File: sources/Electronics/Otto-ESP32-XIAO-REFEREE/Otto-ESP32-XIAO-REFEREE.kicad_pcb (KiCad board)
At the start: 2 copper layers, 60 x 52 mm, 48 parts, among them J1 Industrial Sensor, J12 OLED 0,91" - I2C (SKU21796), J2 Industrial Sensor, J7 Ultrasonic sensor, J8 Barrel_Jack_Switch, SW1 SW_SPDT, SW4 CherryMX, SW5 CherryMX, SW6 CherryMX, U1 MOUDLE-SEEEDUINO-XIAO-ESP32C3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

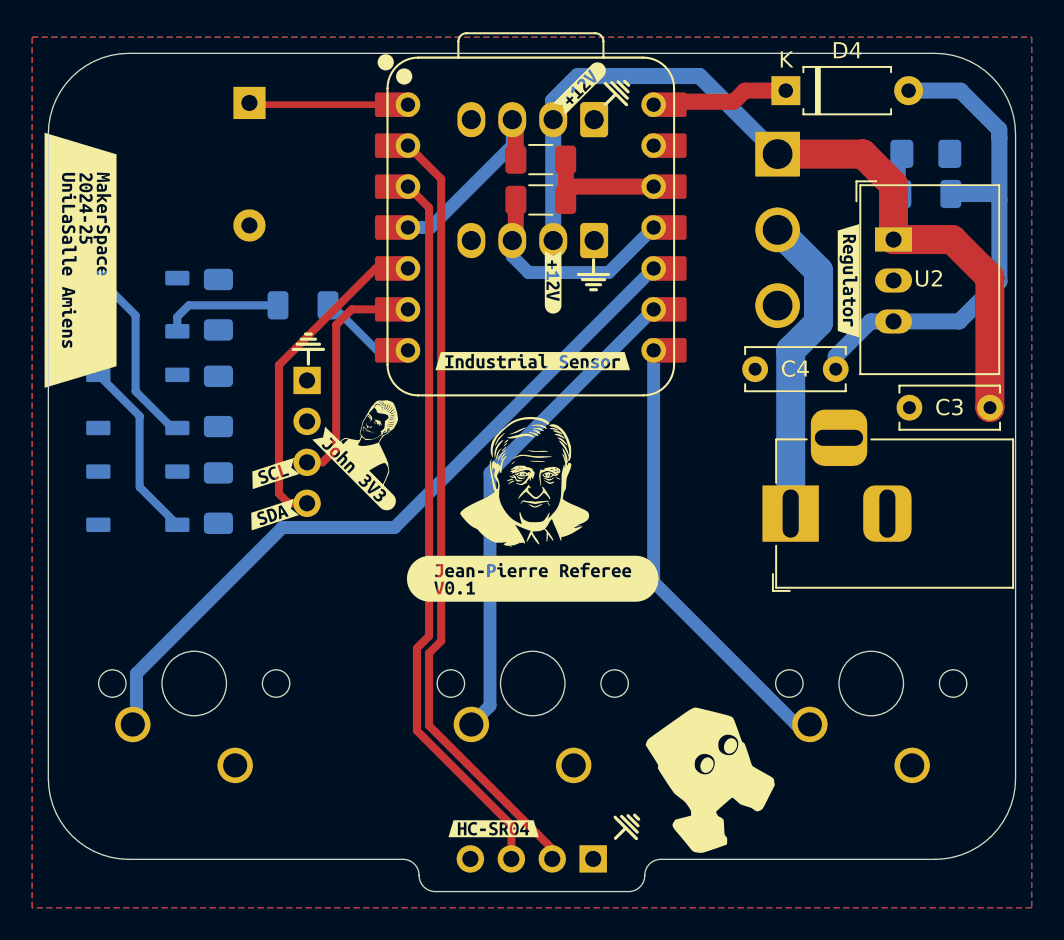
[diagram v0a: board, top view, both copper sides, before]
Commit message: add silkscreen
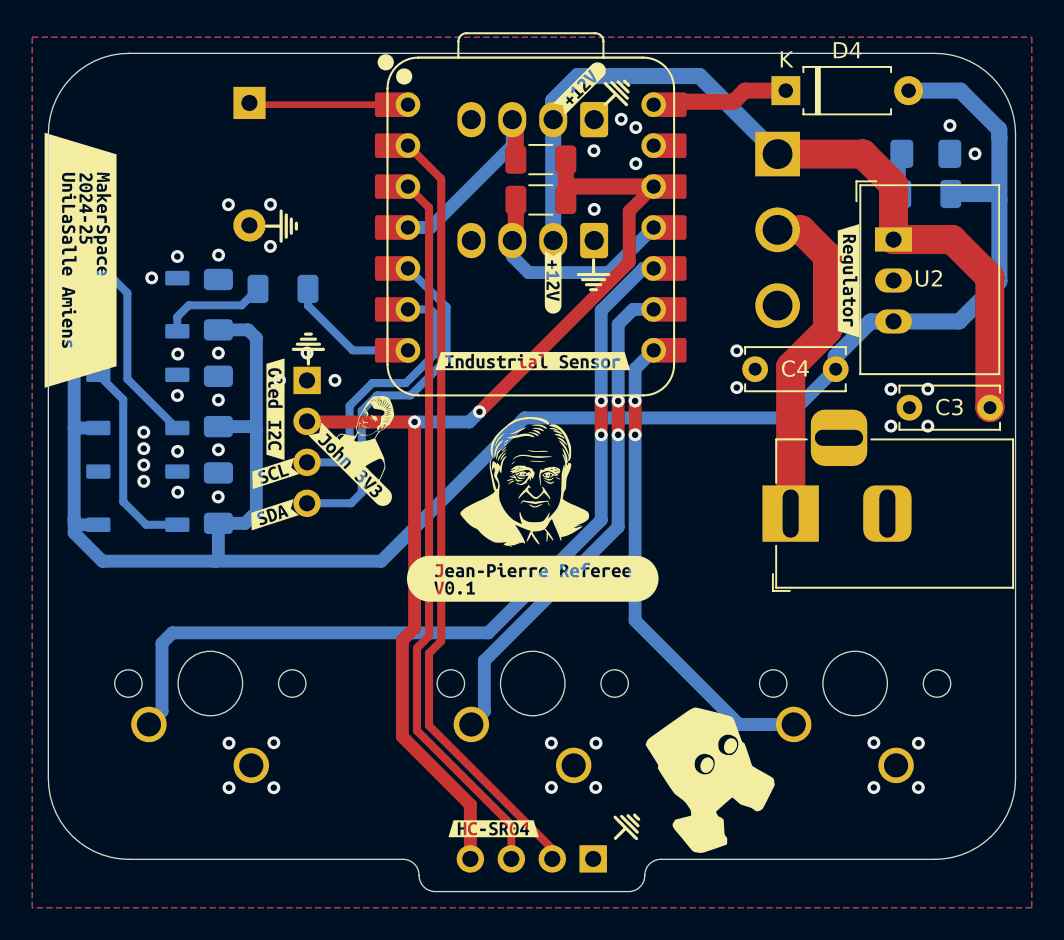
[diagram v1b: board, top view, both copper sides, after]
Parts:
- removed R4: 220, Resistor_SMD:R_1206_3216Metric_Pad1.30x1.75mm_HandSolder
- added G***: LOGO, LOGO, B.Cu at (77.3, 84.4)
- added G***: LOGO, LOGO, B.Cu at (61.7, 89.3)
- added G***: LOGO, LOGO, F.Cu at (57.9, 79.7)
- added R5: 330, Resistor_SMD:R_1206_3216Metric_Pad1.30x1.75mm_HandSolder, B.Cu at (58.0, 83.6)
- added kibuzzard-6765451E: G***, kibuzzard-6765451E, B.Cu at (61.9, 97.6)
- added kibuzzard-67654523: G***, kibuzzard-67654523, B.Cu at (61.8, 95.0)
- added kibuzzard-67E17CB8: G***, kibuzzard-67E17CB8, F.Cu at (57.5, 91.1)
- added kibuzzard-67EAB37B: G***, kibuzzard-67EAB37B, B.Cu at (73.5, 84.6)
- added kibuzzard-67EAB421: G***, kibuzzard-67EAB421, B.Cu at (71.4, 84.6)
- added kibuzzard-67EAB4E0: G***, kibuzzard-67EAB4E0, B.Cu at (62.3, 92.6)
- added kibuzzard-67EAB5AA: G***, kibuzzard-67EAB5AA, B.Cu at (53.2, 115.8)
- added kibuzzard-67EAB5C2: G***, kibuzzard-67EAB5C2, B.Cu at (73.2, 115.7)
- added kibuzzard-67EAB5C7: G***, kibuzzard-67EAB5C7, B.Cu at (93.3, 115.8)
- moved kibuzzard-67E17CA6 11.3 mm to (67.6, 76.9), turned to 90 degrees
- moved SW4 1.00 mm to (96.0, 113.2)
- moved SW6 1.00 mm to (56.0, 113.2)
- moved G*** 0.36 mm to (64.0, 92.7)
- moved kibuzzard-67E17B13 0.36 mm to (62.3, 94.6)
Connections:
- C5 pad 2: +3.3V -> +5V
- C6 pad 2: +3.3V -> +5V
- C7 pad 2: +3.3V -> +5V
- D2 pad 1: +3.3V -> +5V
- D2 pad 4: LED -> Net-(D2-DIN)
- D3 pad 1: +3.3V -> +5V
- D5 pad 1: +3.3V -> +5V
- U1 pad 7: Net-(U1-PB08_A6_D6_TX) -> LED
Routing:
- net +5V: track 31.8 -> 122.5 mm
- net +3.3V: track 8.21 -> 66.8 mm, vias 0 -> 2
- net Key01: track 45.7 -> 53.1 mm, vias 0 -> 2
- net Net-(D2-DIN): track 0.00 -> 6.62 mm
- net Net-(U1-PB08_A6_D6_TX): track 6.12 -> 0.00 mm
- net SCL: track 14.7 -> 16.8 mm
- net Key03: track 27.7 -> 29.7 mm, vias 0 -> 2
- net SDA: track 20.5 -> 22.0 mm
- net Net-(SW1-B): track 19.4 -> 20.7 mm
- net Net-(D3-DOUT): track 11.3 -> 12.5 mm
- net LED: track 7.44 -> 8.39 mm
- net Key02: track 30.4 -> 31.2 mm, vias 0 -> 2
- net GND: vias 0 -> 46

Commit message: add I2C resistors
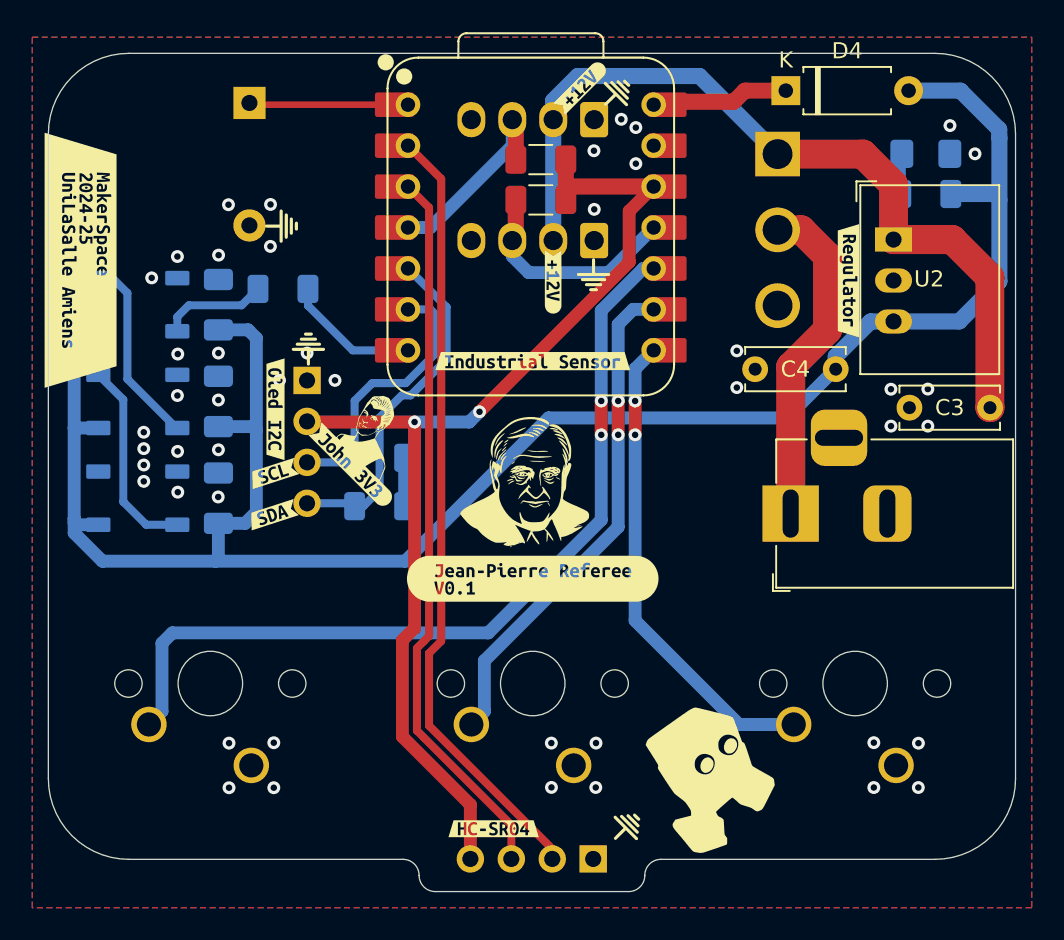
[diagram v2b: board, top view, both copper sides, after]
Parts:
- removed the kibuzzard-6765451E at (61.9, 97.6)
- removed the kibuzzard-67654523 at (61.8, 95.0)
- removed kibuzzard-67EAB4E0: G***, kibuzzard-67EAB4E0
- added R4: 10K, Resistor_SMD:R_1206_3216Metric_Pad1.30x1.75mm_HandSolder, B.Cu at (64.0, 94.1)
- added R6: 10K, Resistor_SMD:R_1206_3216Metric_Pad1.30x1.75mm_HandSolder, B.Cu at (64.0, 97.1)
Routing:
- net +3.3V: track 66.8 -> 72.3 mm
- net SCL: track 16.8 -> 17.4 mm
